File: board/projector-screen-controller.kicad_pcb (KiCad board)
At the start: 2 copper layers, 97.2 x 106 mm, 63 parts, among them J1 ICSP, J2 MSTBVA-3-G, J3 MCV-3-G, J4 MCV-3-G, J5 MCV-3-G, J6 MSTBVA-6-G, J7 MCV-3-G, K1 JS1-12V-F, K2 JS1-12V-F, K3 JS1-12V-F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

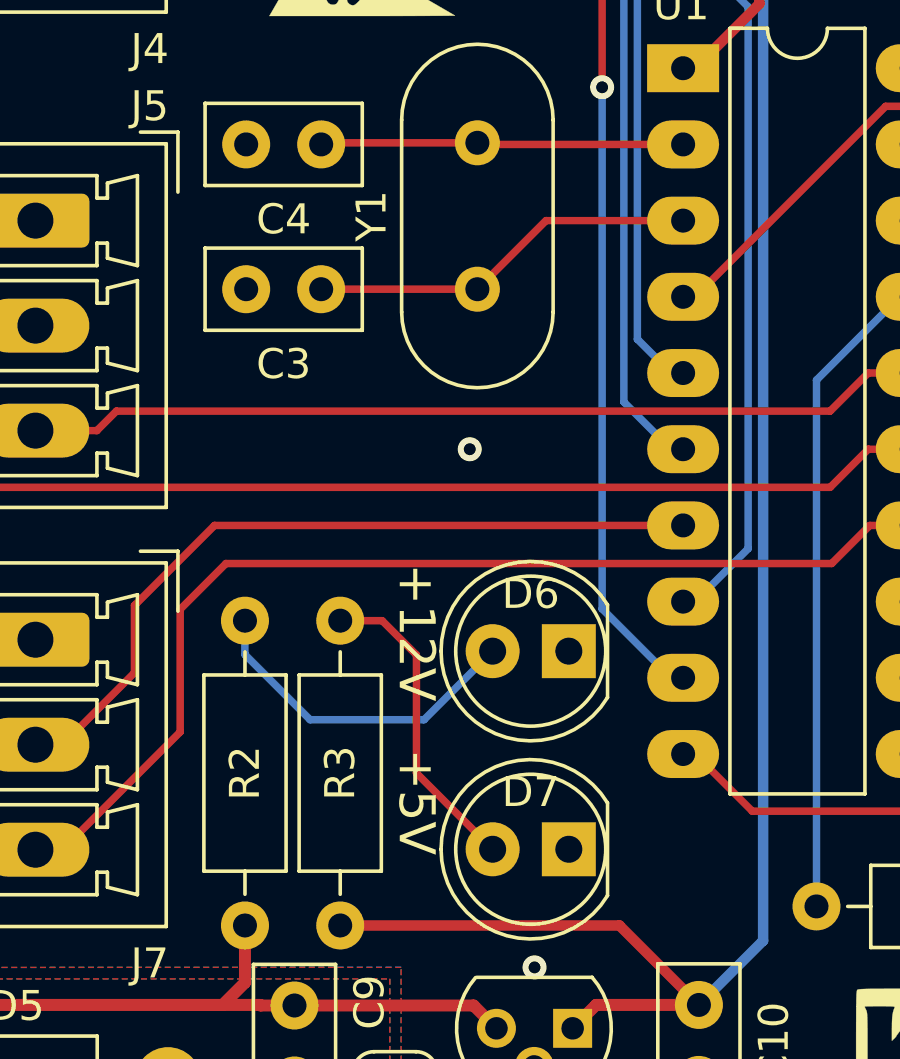
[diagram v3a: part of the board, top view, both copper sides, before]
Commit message: Add/correct a bunch of part numbers
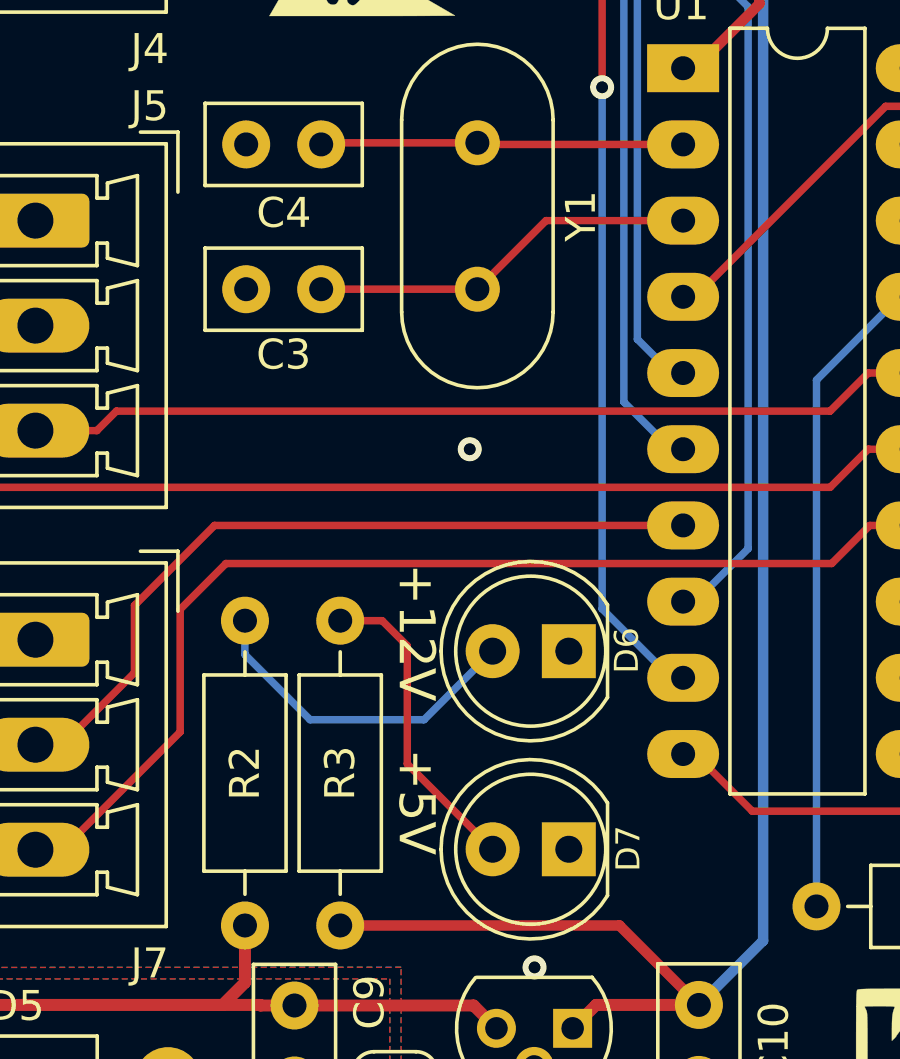
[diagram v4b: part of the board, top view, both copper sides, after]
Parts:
- J2: value MSTBVA-3-G -> MSTBVA 2,5 HC/ 3-G
- J6: value MSTBVA-6-G -> MSTBVA 2,5/ 6-G
- U1: value PIC16F15345-IP -> PIC16F15345-I/P
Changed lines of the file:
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@@
     (descr "Crystal THT HC-49-4H http://5hertz.com/pdfs/04404_D.pdf")
     (tags "THT crystalHC-49-4H")
-    (fp_text reference Y1 (at 2.44 -3.525 90) (layer F.SilkS)
+    (fp_text reference Y1 (at 2.4384 3.4544 90) (layer F.SilkS)
       (effects (font (size 1 1) (thickness 0.15)))
     )
-    (fp_text value 8MHz (at 2.44 3.525 90) (layer F.Fab)
+    (fp_text value 8MHz (at 2.4892 0) (layer F.Fab)
       (effects (font (size 1 1) (thickness 0.15)))
     )
@@
     (fp_line (start -0.76 2.325) (end 5.64 2.325) (layer F.Fab) (width 0.1))
     (fp_line (start -0.76 -2.325) (end 5.64 -2.325) (layer F.Fab) (width 0.1))
-    (fp_text user %R (at 2.44 0 90) (layer F.Fab)
+    (fp_text user %R (at 2.4384 3.4544 90) (layer F.Fab)
       (effects (font (size 1 1) (thickness 0.15)))
     )
@@
     (descr "LED, diameter 5.0mm, 2 pins, http://cdn-reichelt.de/documents/datenblatt/A500/LL-504BC2E-009.pdf")
     (tags "LED diameter 5.0mm 2 pins")
-    (fp_text reference D7 (at 1.27 1.905) (layer F.SilkS)
-      (effects (font (size 1 1) (thickness 0.15)))
+    (fp_text reference D7 (at -1.9812 0.0254 90) (layer F.SilkS)
+      (effects (font (size 0.8 0.8) (thickness 0.15)))
     )
     (fp_text value LED (at 1.27 -1.905) (layer F.Fab)
       (effects (font (size 1 1) (thickness 0.15)))
     )
-    (fp_text user %R (at 1.143 1.905) (layer F.Fab)
-      (effects (font (size 0.8 0.8) (thickness 0.2)))
+    (fp_text user %R (at -1.9812 0.0254 90) (layer F.Fab)
+      (effects (font (size 0.8 0.8) (thickness 0.15)))
     )
     (fp_line (start 4.5 -3.25) (end -1.95 -3.25) (layer F.CrtYd) (width 0.05))
@@
     (descr "LED, diameter 5.0mm, 2 pins, http://cdn-reichelt.de/documents/datenblatt/A500/LL-504BC2E-009.pdf")
     (tags "LED diameter 5.0mm 2 pins")
-    (fp_text reference D6 (at 1.27 1.905) (layer F.SilkS)
-      (effects (font (size 1 1) (thickness 0.15)))
+    (fp_text reference D6 (at -1.9304 0.0254 90) (layer F.SilkS)
+      (effects (font (size 0.8 0.8) (thickness 0.15)))
     )
     (fp_text value LED (at 1.397 -1.778) (layer F.Fab)
       (effects (font (size 1 1) (thickness 0.15)))
     )
-    (fp_text user %R (at 1.25 1.778) (layer F.Fab)
-      (effects (font (size 0.8 0.8) (thickness 0.2)))
+    (fp_text user %R (at -1.9304 0.0254 90) (layer F.Fab)
+      (effects (font (size 0.8 0.8) (thickness 0.15)))
     )
     (fp_line (start 4.5 -3.25) (end -1.95 -3.25) (layer F.CrtYd) (width 0.05))
@@
       (effects (font (size 1 1) (thickness 0.15)))
     )
-    (fp_text value 0.1uF (at 1.25 2.5) (layer F.Fab)
+    (fp_text value 0.1uF (at 4.6736 -0.6858 90) (layer F.Fab)
       (effects (font (size 1 1) (thickness 0.15)))
     )
@@
     (descr "C, Disc series, Radial, pin pitch=2.50mm, , diameter*width=5*2.5mm^2, Capacitor, http://cdn-reichelt.de/documents/datenblatt/B300/DS_KERKO_TC.pdf")
     (tags "C Disc series Radial pin pitch 2.50mm  diameter 5mm width 2.5mm Capacitor")
-    (fp_text reference C4 (at 1.25 -2.5) (layer F.SilkS)
+    (fp_text reference C4 (at 1.2446 -2.286) (layer F.SilkS)
       (effects (font (size 1 1) (thickness 0.15)))
     )
@@
       (effects (font (size 1 1) (thickness 0.15)))
     )
-    (fp_text user %R (at 1.27 -2.54) (layer F.Fab)
+    (fp_text user %R (at 1.2446 -2.286) (layer F.Fab)
       (effects (font (size 1 1) (thickness 0.15)))
     )
@@
     (descr "C, Disc series, Radial, pin pitch=2.50mm, , diameter*width=5*2.5mm^2, Capacitor, http://cdn-reichelt.de/documents/datenblatt/B300/DS_KERKO_TC.pdf")
     (tags "C Disc series Radial pin pitch 2.50mm  diameter 5mm width 2.5mm Capacitor")
-    (fp_text reference C3 (at 1.25 -2.5) (layer F.SilkS)
+    (fp_text reference C3 (at 1.25 -2.1844) (layer F.SilkS)
       (effects (font (size 1 1) (thickness 0.15)))
     )
@@
       (effects (font (size 1 1) (thickness 0.15)))
     )
-    (fp_text user %R (at 1.25 -2.794) (layer F.Fab)
+    (fp_text user %R (at 1.2446 -2.1844) (layer F.Fab)
       (effects (font (size 1 1) (thickness 0.15)))
     )
@@
       (effects (font (size 1 1) (thickness 0.15)))
     )
-    (fp_text value PIC16F15345-IP (at 2.54 17.78 90) (layer F.Fab)
+    (fp_text value PIC16F15345-I/P (at 2.54 17.78 90) (layer F.Fab)
       (effects (font (size 1 1) (thickness 0.15)))
     )
@@
       (effects (font (size 1 1) (thickness 0.15)))
     )
-    (fp_text value MSTBVA-6-G (at 12.5 -4.445 90) (layer F.Fab)
+    (fp_text value "MSTBVA 2,5/ 6-G" (at 12.5 -4.445 90) (layer F.Fab)
       (effects (font (size 1 1) (thickness 0.15)))
     )
@@
       (effects (font (size 1 1) (thickness 0.15)))
     )
-    (fp_text value MSTBVA-3-G (at 4.445 -4.445 90) (layer F.Fab)
+    (fp_text value "MSTBVA 2,5 HC/ 3-G" (at 4.445 -4.445 90) (layer F.Fab)
       (effects (font (size 1 1) (thickness 0.15)))
     )
@@
   (segment (start 95.504 105.537) (end 97.79 103.251) (width 0.25) (layer B.Cu) (net 51) (status 20))
   (segment (start 91.70563 105.537) (end 95.504 105.537) (width 0.25) (layer B.Cu) (net 51))
-  (segment (start 95.25 107.315) (end 97.79 109.855) (width 0.25) (layer F.Cu) (net 52) (status 20))
-  (segment (start 95.25 103.378) (end 95.25 107.315) (width 0.25) (layer F.Cu) (net 52))
-  (segment (start 92.71 102.235) (end 94.107 102.235) (width 0.25) (layer F.Cu) (net 52) (status 10))
-  (segment (start 94.107 102.235) (end 95.25 103.378) (width 0.25) (layer F.Cu) (net 52))
+  (segment (start 94.9452 107.0102) (end 97.79 109.855) (width 0.25) (layer F.Cu) (net 52))
+  (segment (start 94.9452 103.0732) (end 94.9452 107.0102) (width 0.25) (layer F.Cu) (net 52))
+  (segment (start 92.71 102.235) (end 94.107 102.235) (width 0.25) (layer F.Cu) (net 52))
+  (segment (start 94.107 102.235) (end 94.9452 103.0732) (width 0.25) (layer F.Cu) (net 52))
   (segment (start 118.745 62.357) (end 118.745 62.865) (width 0.25) (layer F.Cu) (net 53) (status 30))
   (segment (start 121.92 59.182) (end 118.745 62.357) (width 0.25) (layer F.Cu) (net 53) (status 30))

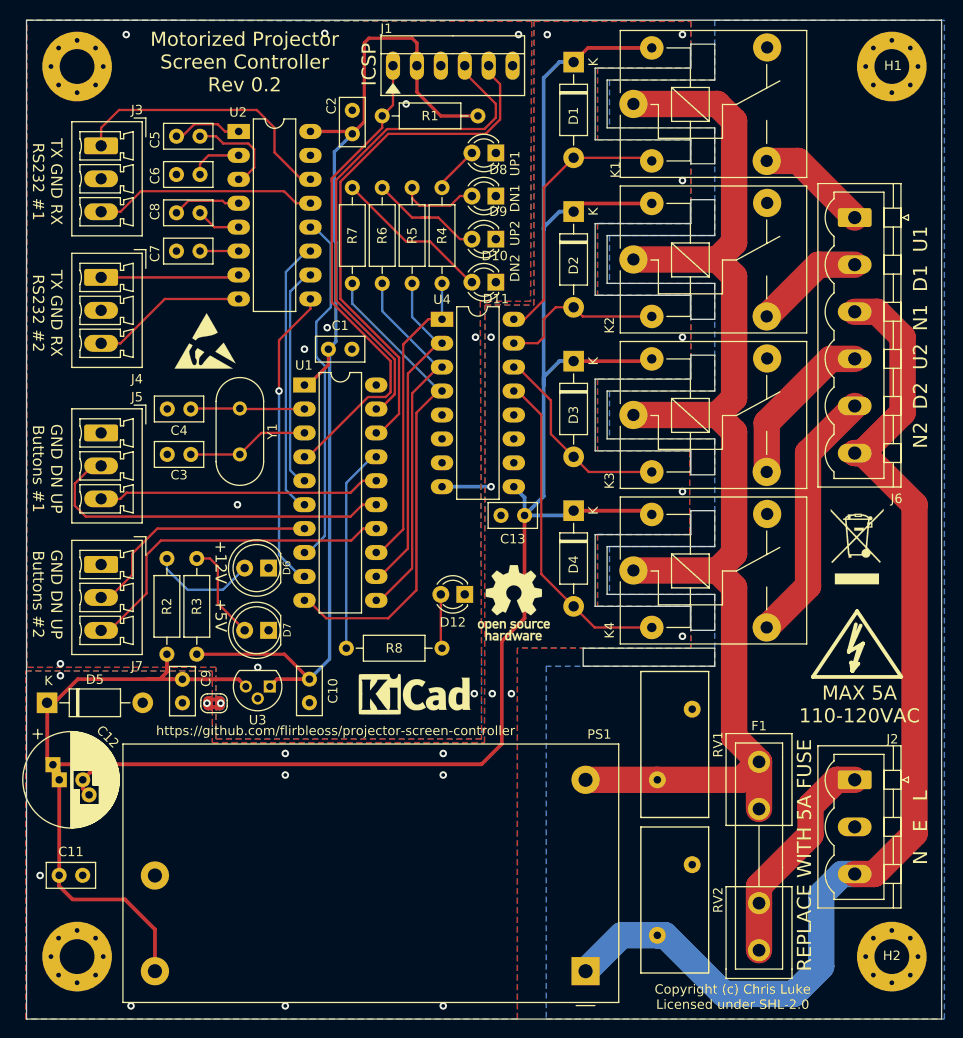
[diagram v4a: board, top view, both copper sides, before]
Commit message: Layout adjustments to make room
* Move the relays and diodes left to give a little more room to the
  power connectors; adjust ground planes to suit, etc.
* Larger footprint for TVS diode; related adjustments.
* Other minor adjustments to layout.
* Add board-only preview.
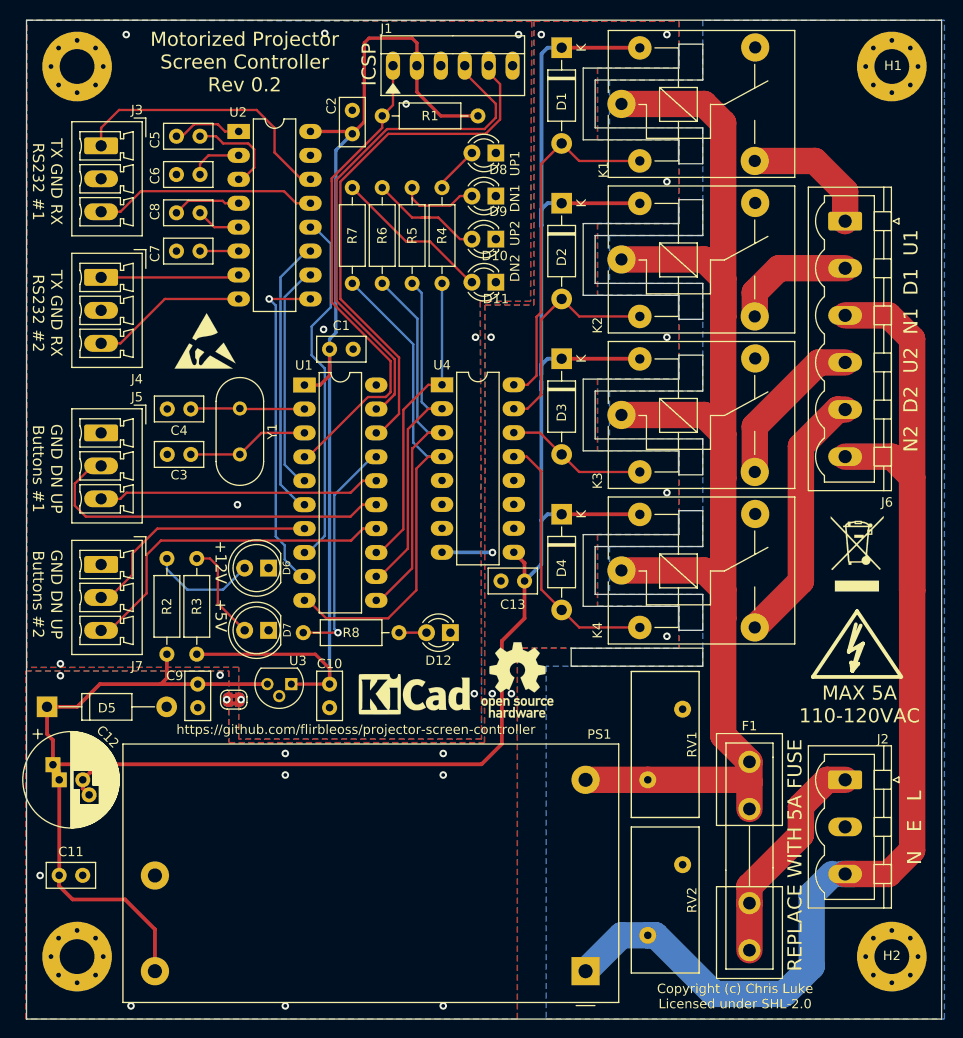
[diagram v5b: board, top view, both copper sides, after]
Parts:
- D5: footprint Diode_THT:D_DO-41_SOD81_P10.16mm_Horizontal -> Diodes_THT:D_DO-41_SOD81_P12.70mm_Horizontal
- moved REF*** 8.20 mm to (126.7, 115.1)
- moved C13 6.96 mm to (127.5, 104.6)
- moved U4 6.96 mm to (118.7, 83.8)
- moved R8 4.86 mm to (104.0, 110.1)
- moved D12 4.34 mm to (119.6, 110.1)
- moved U3 2.30 mm to (102.7, 115.6)
- moved C10 2.20 mm to (106.8, 115.6)
- moved JP1 2.13 mm to (96.6, 117.2)
- moved JP2 2.10 mm to (96.6, 117.2)
- moved D1 1.98 mm to (131.4, 48.0)
- moved C9 1.70 mm to (92.8, 115.6)
- moved D2 1.55 mm to (131.4, 64.5)
- moved D4 1.33 mm to (131.4, 97.5)
- moved D3 1.30 mm to (131.4, 81.0)
- moved K1 1.27 mm to (137.8, 54.0)
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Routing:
- net NEUT: track 115.2 -> 132.1 mm
- net LINE: track 135.9 -> 149.9 mm
- net Net-(D1-Pad2): track 28.9 -> 38.1 mm
- net Net-(D4-Pad2): track 35.0 -> 28.3 mm
- net Net-(D3-Pad2): track 21.4 -> 15.1 mm
- net Net-(D2-Pad2): track 17.7 -> 23.7 mm
- net Net-(U1-Pad9): track 32.2 -> 36.2 mm
- net +5V: track 116.2 -> 119.7 mm
- net Net-(D12-Pad2): track 5.77 -> 2.92 mm
- net Net-(R8-Pad1): track 21.9 -> 24.6 mm, vias 0 -> 1
- net /Relay/D1_UP_AC: track 11.8 -> 14.1 mm
- net +12V: track 241.3 -> 239.2 mm
- net /MCU/D2_UP_TTL: track 39.1 -> 41.2 mm
- net /MCU/D2_DN_TTL: track 51.3 -> 53.3 mm
- net /MCU/D1_DN_TTL: track 35.6 -> 37.3 mm
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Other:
- outline, holes or cut-outs redrawn
